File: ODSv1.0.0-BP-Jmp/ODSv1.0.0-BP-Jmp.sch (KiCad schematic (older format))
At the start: 4 parts

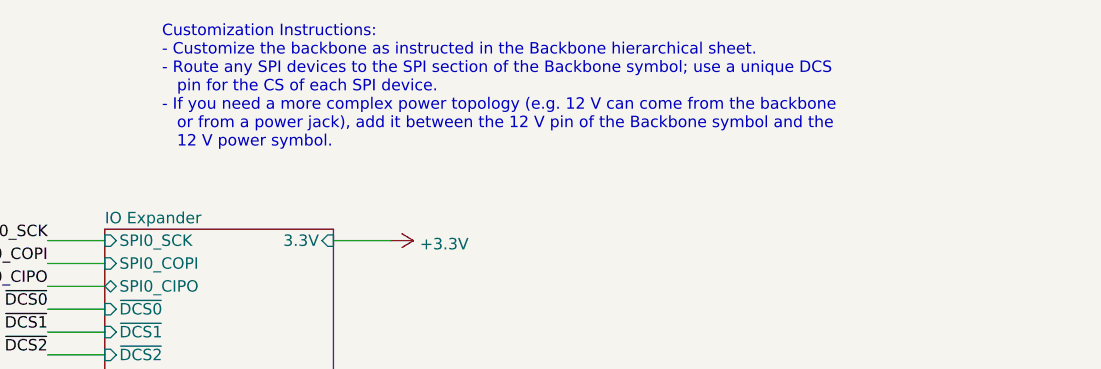
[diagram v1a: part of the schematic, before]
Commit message: Replace DAC with a second MAX7317 expander with pullup resistors
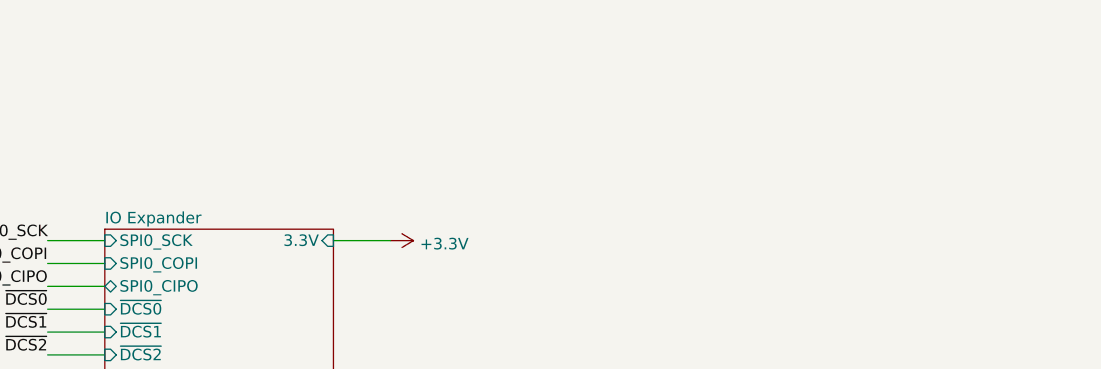
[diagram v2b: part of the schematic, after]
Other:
- note removed: "Customization Instructions:\n- Customize the backbone as instructed in the Backbone hierarchical sheet.\n- Route any SPI devices to the SPI section of the Backbone symbol; use a unique DCS\n pin for the CS of each SPI device.\n- If you need a more complex power topology (e.g. 12 V can come from the backbone\n or from a power jack), add it between the 12 V pin of the Backbone symbol and the\n 12 V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"
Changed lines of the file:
@@
 	0    1    1    0
 $EndComp
-Text Notes 7000 1100 0    50   ~ 0
-Customization Instructions:\n- Customize the backbone as instructed in the Backbone hierarchical sheet.\n- Route any SPI devices to the SPI section of the Backbone symbol; use a unique DCS\n   pin for the CS of each SPI device.\n- If you need a more complex power topology (e.g. 12 V can come from the backbone\n   or from a power jack), add it between the 12 V pin of the Backbone symbol and the\n   12 V power symbol.
 $Comp
 L Mechanical:MountingHole H1
